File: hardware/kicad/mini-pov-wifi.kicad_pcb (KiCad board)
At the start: 2 copper layers, 28 x 118 mm, 24 parts, among them J2 USB-C, U1 MT3608, U2 Wemos_D1_Mini

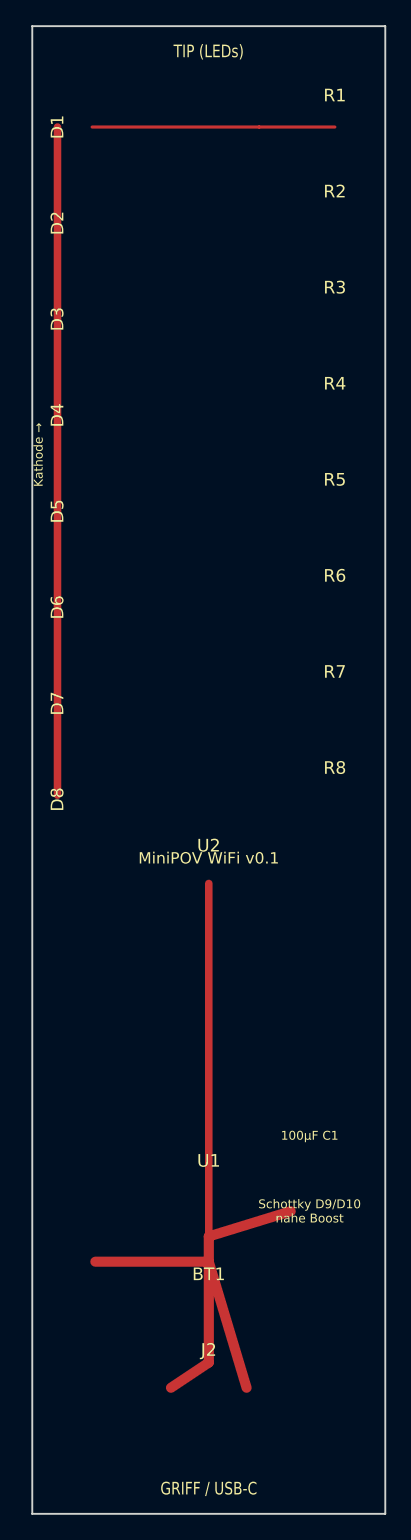
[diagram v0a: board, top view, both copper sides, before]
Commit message: Fix KiCad PCB syntax: remove invalid comments and embed footprint pads.
Co-authored-by: Cursor <cursoragent@cursor.com>
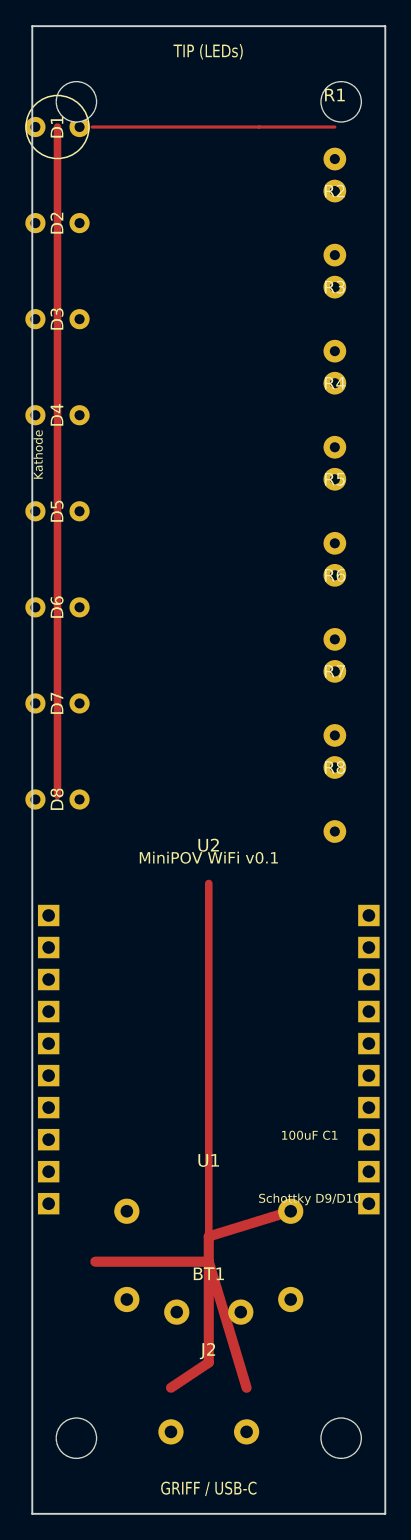
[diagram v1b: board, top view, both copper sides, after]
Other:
- board text added: "100uF C1"
- board text added: "Kathode"
- board text added: "Schottky D9/D10"
- board text removed: "100µF C1"
- board text removed: "Kathode →"
- board text removed: "Schottky D9/D10 nahe Boost"
